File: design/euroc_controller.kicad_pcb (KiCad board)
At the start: 4 copper layers, 35.1 x 75.7 mm, 86 parts, among them J1 xt30, J2 jst_sh 4, J4 jst_sh 4, J5 jst_sh 4, J6 SMA, J7 Screw_Terminal_01x06, J8 USB_C_Receptacle_USB2.0, J9 jst_sh 4, Q1 MMBT3904, U1 TPSM5601R5, U10 VN7050ASTR, U11 VN7050ASTR, U13 STM32U575CGTx, U2 USBLC6-2SC6, U3 LSM6DSO32, U4 MS5611-01BA, U5 SN65HVD232, U6 W25Q128JVS, U7 RFM69W, U8 L86, U9 VN7050ASTR, Y1 48MHz

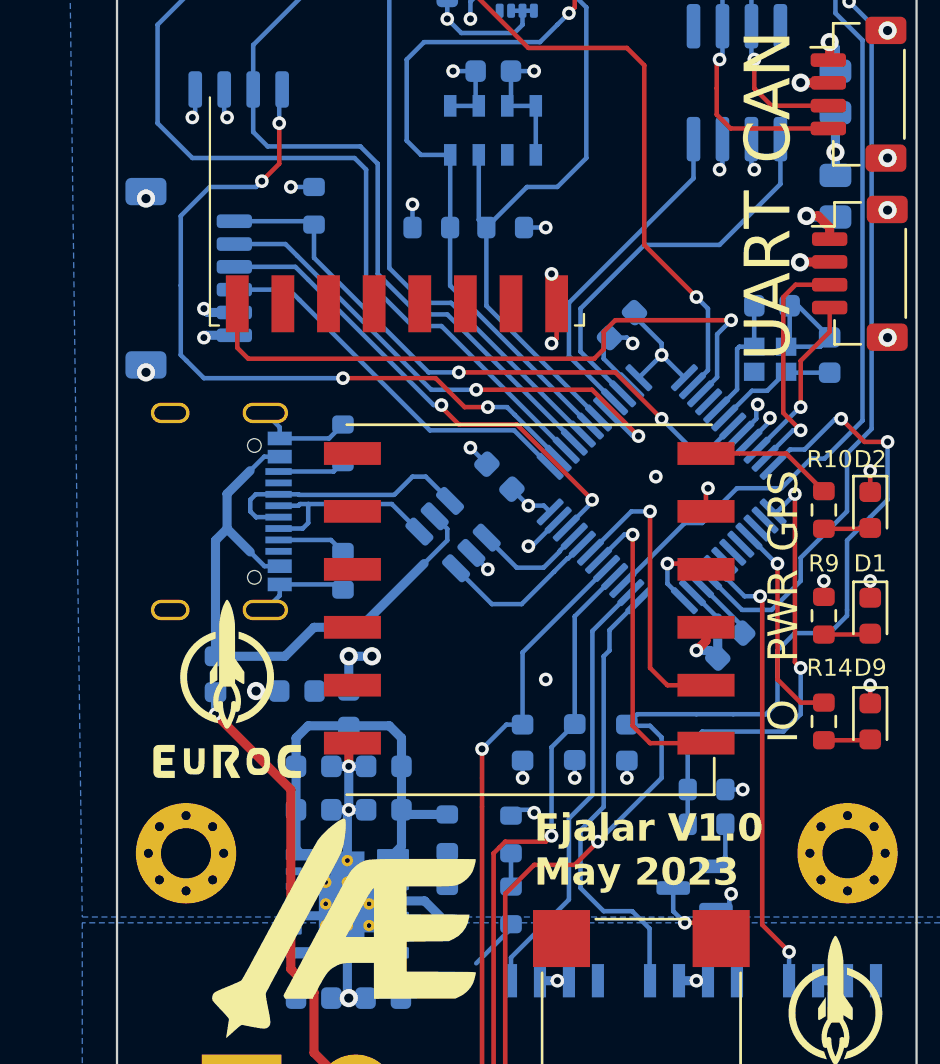
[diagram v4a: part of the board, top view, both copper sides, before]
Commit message: can transceiver, decoupling caps
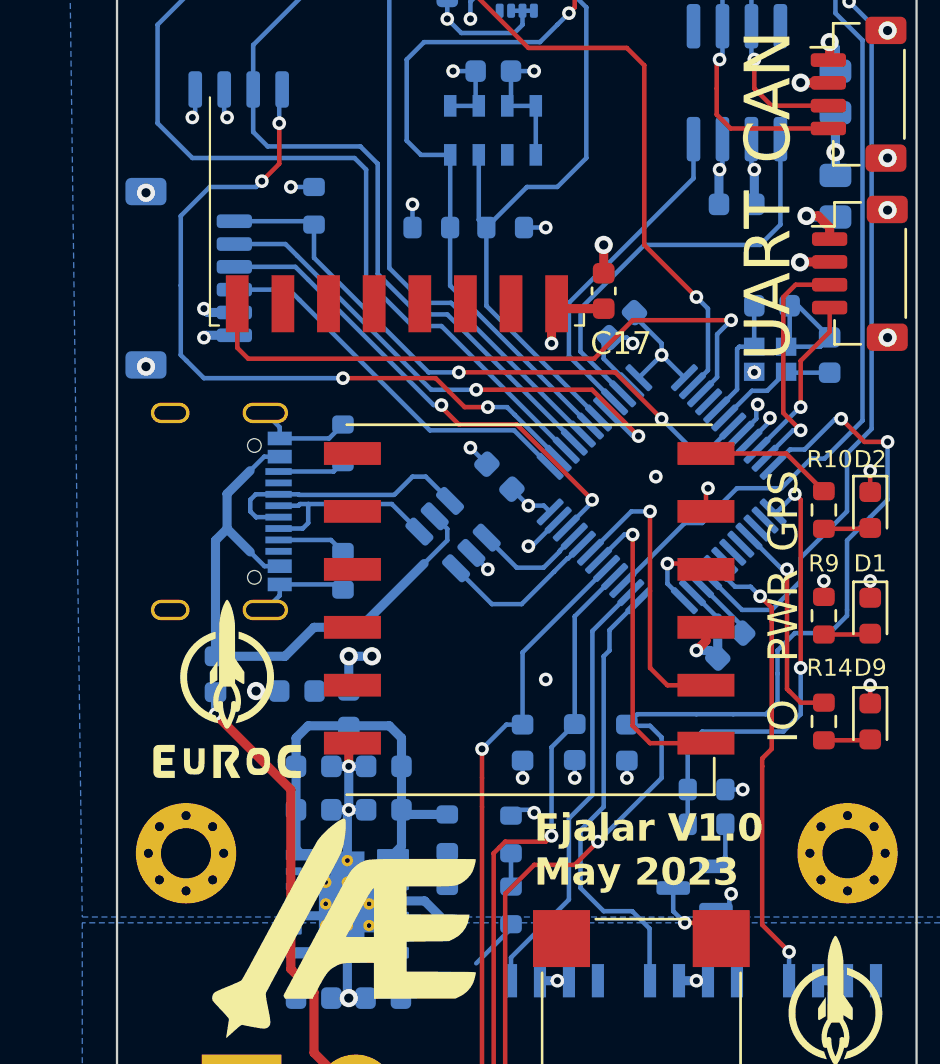
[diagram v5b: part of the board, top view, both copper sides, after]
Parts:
- added C16: 0.1u, Capacitor_SMD:C_0603_1608Metric, B.Cu at (191.5, 69.1)
- added C17: 0.1u, Capacitor_SMD:C_0603_1608Metric, F.Cu at (185.7, 72.9)
- U5: value SN65HVD232 -> TCAN332
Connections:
- Y1 pad 4: unconnected-(Y1-Pad4) -> Earth
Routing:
- net Earth: track 101.9 -> 105.6 mm, vias 43 -> 45
- net +3V3: track 55.8 -> 58.1 mm, vias 24 -> 23
- net /CAN_TX: track 17.5 -> 18.5 mm

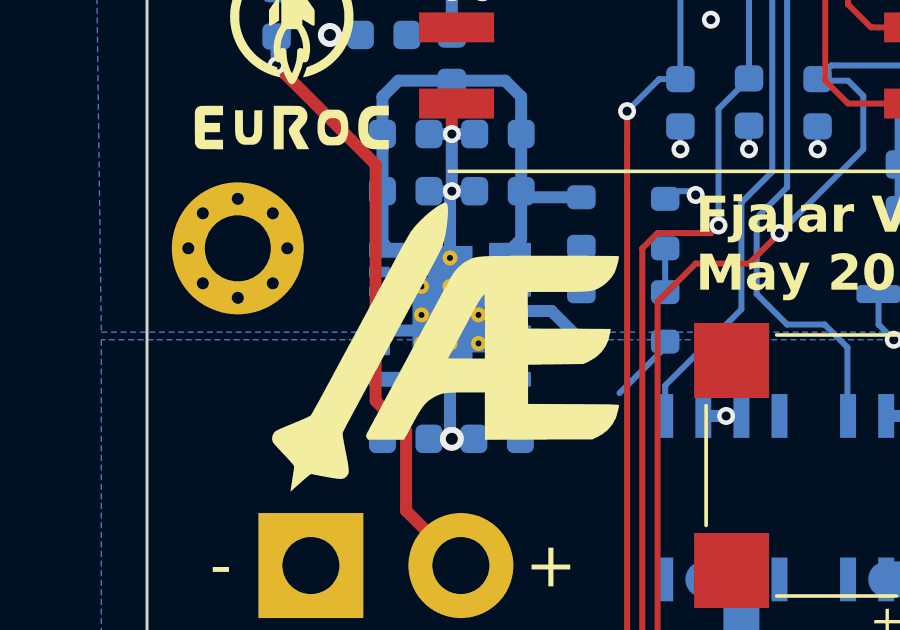
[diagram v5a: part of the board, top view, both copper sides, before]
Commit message: fix aesir logo
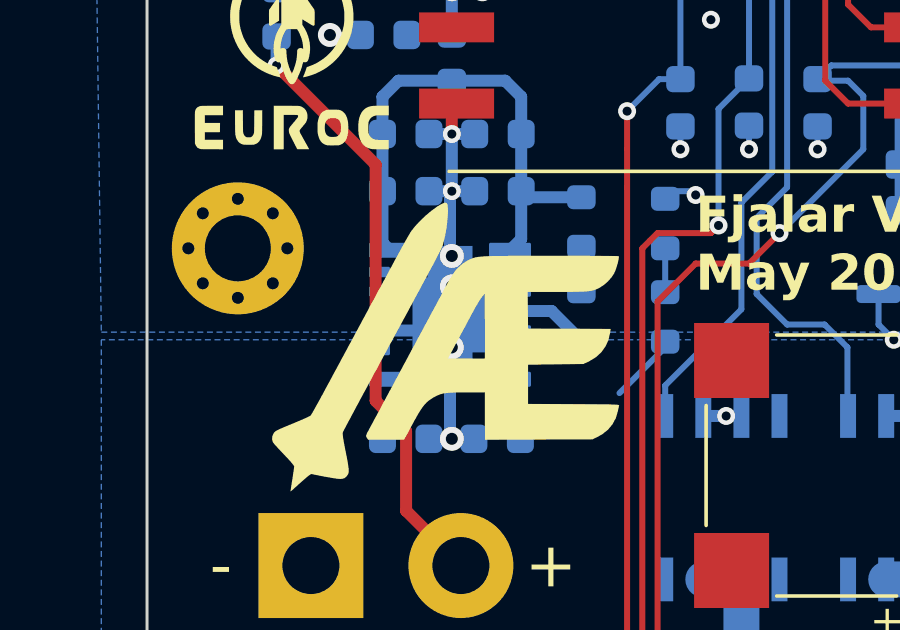
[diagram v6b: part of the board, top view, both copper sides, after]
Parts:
- U1: footprint Package_DFN_QFN:Texas_B3QFN-14-1EP_5x5.5mm_P0.65mm_ThermalVia -> Package_DFN_QFN:Texas_B3QFN-14-1EP_5x5.5mm_P0.65mm
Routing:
- net Earth: track 105.6 -> 106.0 mm, vias 45 -> 50

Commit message: better sma
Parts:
- J6: footprint Connector_Coaxial:SMA_Molex_73251-1153_EdgeMount_Horizontal -> Connector_Coaxial:SMA_Amphenol_901-143_Horizontal
- moved H1 2.00 mm to (167.4, 47.5)
- moved H2 2.00 mm to (196.4, 47.5)
- moved J6 1.29 mm to (181.9, 49.1), turned to 0 degrees
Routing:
- net Earth: track 106.0 -> 105.4 mm
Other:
- board size 35.1 x 75.7 mm -> 35.1 x 77 mm

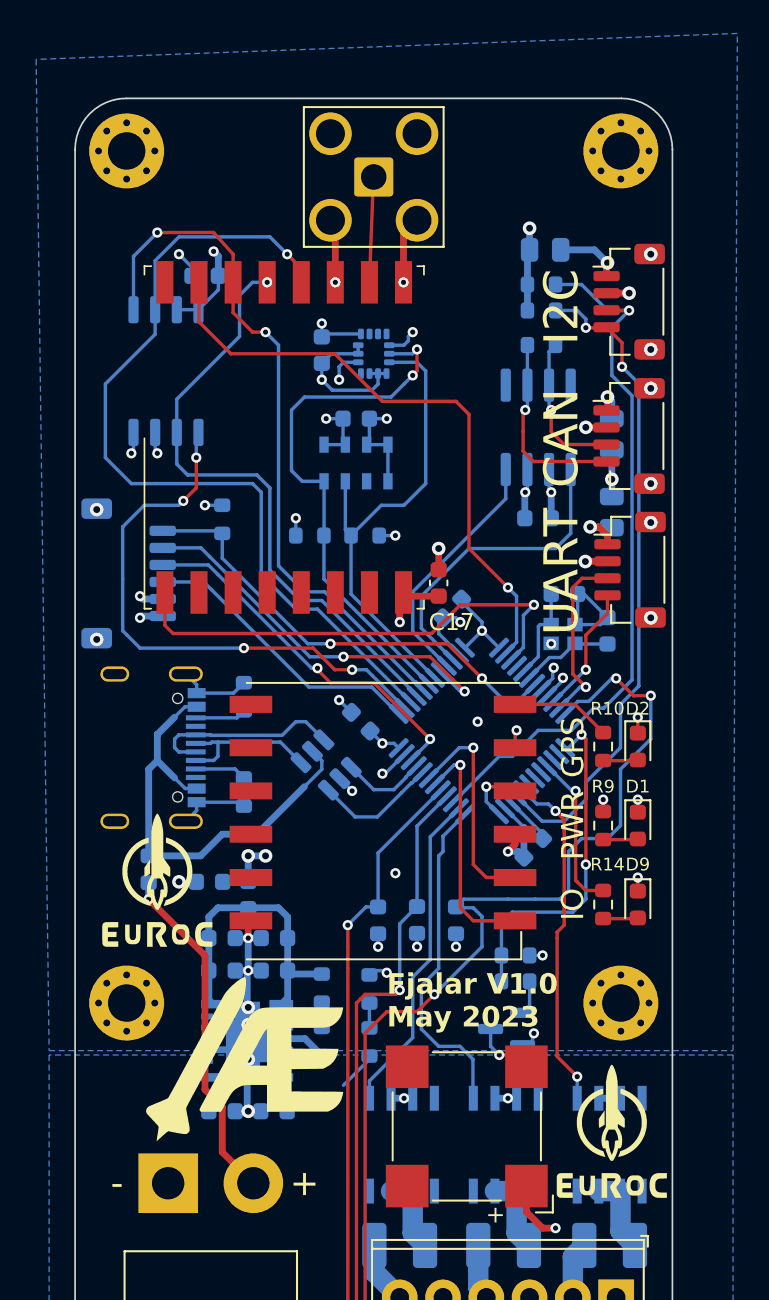
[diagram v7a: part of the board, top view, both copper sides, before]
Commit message: route dp
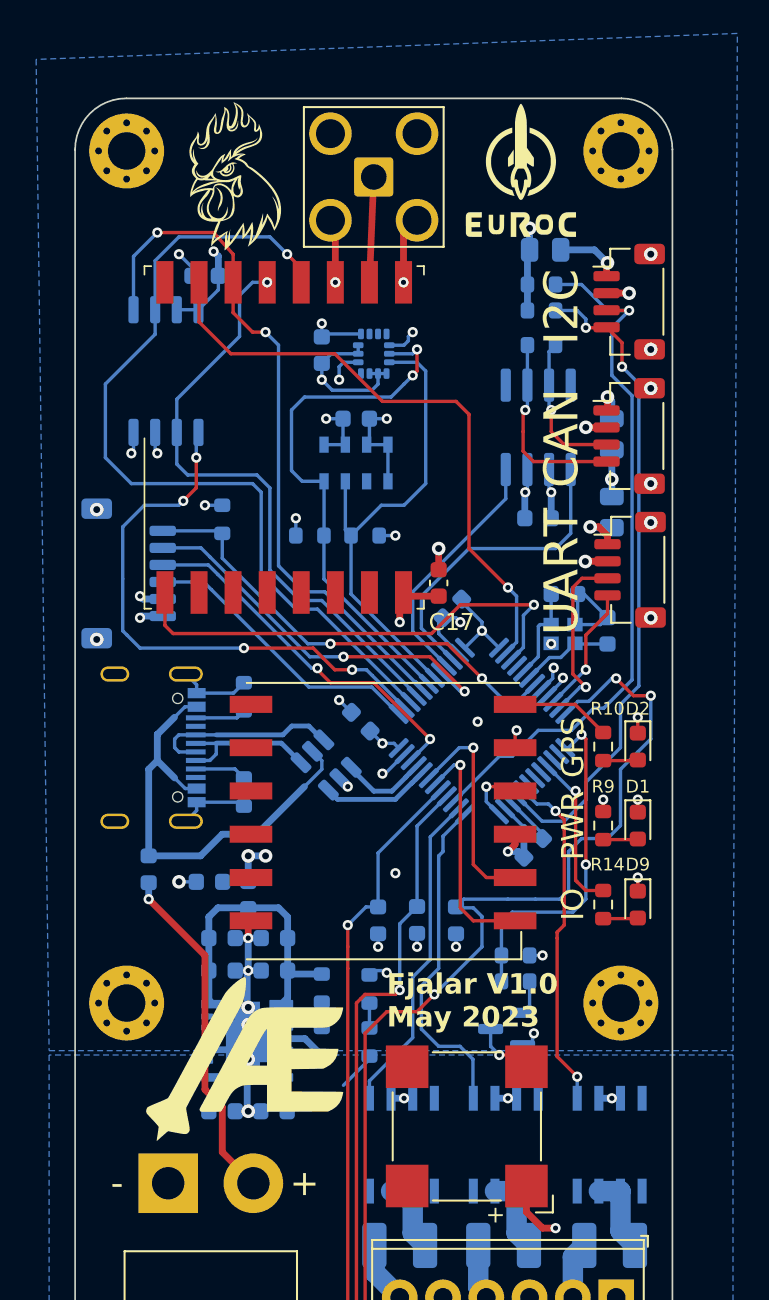
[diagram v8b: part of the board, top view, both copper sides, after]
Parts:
- removed the G*** at (169.2, 90.4)
- removed the G*** at (195.8, 105.2)
- removed the G*** at (172.5, 114.6)
- added G***: LOGO, lib:rooster3, F.Cu at (173.7, 49.0)
- added G***: LOGO, lib:euroc, F.Cu at (190.5, 48.8)
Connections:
- net Net-(J6-In) renamed /LORA
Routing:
- net /USB_D_N: track 7.28 -> 6.43 mm
